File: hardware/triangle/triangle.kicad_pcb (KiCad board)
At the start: 4 copper layers, 100 x 86.6 mm, 60 parts, among them J1 Conn_01x02_Socket, J2 Conn_01x02_Socket

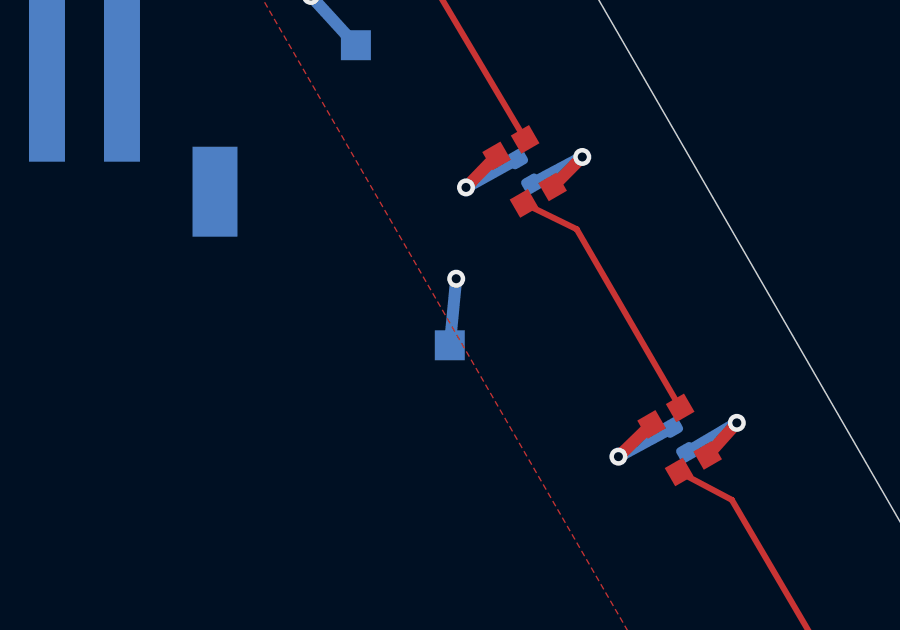
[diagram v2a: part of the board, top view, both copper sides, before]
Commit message: remove unnecessary test pad and add silkscreen for sockets
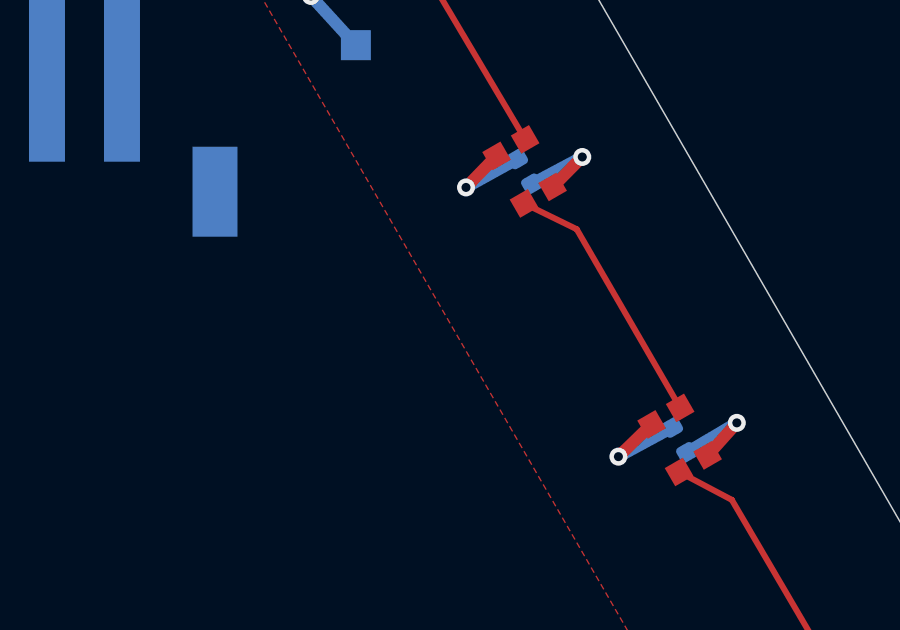
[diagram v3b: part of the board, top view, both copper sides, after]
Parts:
- removed TP2-GND1: TestPoint, TestPoint:TestPoint_Pad_1.0x1.0mm
- renumbered TP3-LED_DATA_IN1 to TP2-LED_DATA_IN1, TP4-LED_DATA_OUT1 to TP3-LED_DATA_OUT1
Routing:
- net GND: track 85.9 -> 83.7 mm, vias 26 -> 25
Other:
- board text added: "DATA"
- board text added: "POWER"
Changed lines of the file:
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@@
 		(descr "SMD rectangular pad as test Point, square 1.0mm side length")
 		(tags "test point SMD pad rectangle square")
-		(property "Reference" "TP3-LED_DATA_IN1"
-			(at 2.14597 2.509828 180)
+		(property "Reference" "TP2-LED_DATA_IN1"
+			(at 7.768737 2.304963 180)
 			(layer "B.SilkS")
 			(effects
@@
 		)
 	)
-	(footprint "TestPoint:TestPoint_Pad_1.0x1.0mm"
-		(layer "B.Cu")
-		(at 168.177353 114.994019)
-		(descr "SMD rectangular pad as test Point, square 1.0mm side length")
-		(tags "test point SMD pad rectangle square")
-		(property "Reference" "TP2-GND1"
-			(at 0 1.448 180)
-			(layer "B.SilkS")
-			(effects
-				(font
-					(size 1 1)
-					(thickness 0.15)
-				)
-				(justify mirror)
-			)
-		)
-		(property "Value" "TestPoint"
-			(at 0 -1.55 180)
-			(layer "B.Fab")
-			(effects
-				(font
-					(size 1 1)
-					(thickness 0.15)
-				)
-				(justify mirror)
-			)
-		)
-		(property "Datasheet" ""
-			(at 0 0 180)
-			(unlocked yes)
-			(layer "B.Fab")
-			(hide yes)
-			(effects
-				(font
-					(size 1.27 1.27)
-					(thickness 0.15)
-				)
-				(justify mirror)
-			)
-		)
-		(property "Description" "test point"
-			(at 0 0 180)
-			(unlocked yes)
-			(layer "B.Fab")
-			(hide yes)
-			(effects
-				(font
-					(size 1.27 1.27)
-					(thickness 0.15)
-				)
-				(justify mirror)
-			)
-		)
-		(property ki_fp_filters "Pin* Test*")
-		(sheetname "/")
-		(sheetfile "triangle.kicad_sch")
-		(units
-			(unit
-				(name "A")
-				(pins "1")
-			)
-		)
-		(duplicate_pad_numbers_are_jumpers no)
-		(fp_line
-			(start -0.7 -0.7)
-			(end -0.7 0.7)
-			(stroke
-				(width 0.12)
-				(type solid)
-			)
-			(layer "B.SilkS")
-		)
-		(fp_line
-			(start -0.7 0.7)
-			(end 0.7 0.7)
-			(stroke
-				(width 0.12)
-				(type solid)
-			)
-			(layer "B.SilkS")
-		)
-		(fp_line
-			(start 0.7 -0.7)
-			(end -0.7 -0.7)
-			(stroke
-				(width 0.12)
-				(type solid)
-			)
-			(layer "B.SilkS")
-		)
-		(fp_line
-			(start 0.7 0.7)
-			(end 0.7 -0.7)
-			(stroke
-				(width 0.12)
-				(type solid)
-			)
-			(layer "B.SilkS")
-		)
-		(fp_line
-			(start -1 1)
-			(end -1 -1)
-			(stroke
-				(width 0.05)
-				(type solid)
-			)
-			(layer "B.CrtYd")
-		)
-		(fp_line
-			(start -1 1)
-			(end 1 1)
-			(stroke
-				(width 0.05)
-				(type solid)
-			)
-			(layer "B.CrtYd")
-		)
-		(fp_line
-			(start 1 -1)
-			(end -1 -1)
-			(stroke
-				(width 0.05)
-				(type solid)
-			)
-			(layer "B.CrtYd")
-		)
-		(fp_line
-			(start 1 -1)
-			(end 1 1)
-			(stroke
-				(width 0.05)
-				(type solid)
-			)
-			(layer "B.CrtYd")
-		)
-		(fp_text user "${REFERENCE}"
-			(at 0 1.45 180)
-			(layer "B.Fab")
-			(effects
-				(font
-					(size 1 1)
-					(thickness 0.15)
-				)
-				(justify mirror)
-			)
-		)
-		(pad "1" smd rect
-			(at 0 0)
-			(size 1 1)
-			(layers "B.Cu" "B.Mask")
-			(net "GND")
-			(pinfunction "1_1")
-			(pintype "passive")
-		)
-		(embedded_fonts no)
-	)
 	(footprint "footprints:CONN-SMD_B2B-PH-SM4-TBT-LF-SN"
 		(layer "B.Cu")
@@
 				(font
 					(size 1.27 1.27)
+					(thickness 0.15)
 				)
 			)
@@
 				(font
 					(size 1.27 1.27)
+					(thickness 0.15)
 				)
 			)
@@
 		(descr "SMD rectangular pad as test Point, square 1.0mm side length")
 		(tags "test point SMD pad rectangle square")
-		(property "Reference" "TP4-LED_DATA_OUT1"
+		(property "Reference" "TP3-LED_DATA_OUT1"
 			(at 9.150116 0.172102 180)
 			(layer "B.SilkS")
@@
 		(layer "Edge.Cuts")
 	)
+	(gr_text "DATA"
+		(at 138.826309 123.211051 0)
+		(layer "B.SilkS")
+		(effects
+			(font
+				(size 1.5 1.5)
+				(thickness 0.3)
+				(bold yes)
+			)
+			(justify left bottom mirror)
+		)
+	)
+	(gr_text "POWER"
+		(at 159.990256 114.835091 0)
+		(layer "B.SilkS")
+		(effects
+			(font
+				(size 1.5 1.5)
+				(thickness 0.3)
+				(bold yes)
+			)
+			(justify left bottom mirror)
+		)
+	)
 	(segment
 		(start 116.350567 141.095301)
@@
 	)
 	(via
-		(at 168.390091 112.775809)
-		(size 0.6)
-		(drill 0.3)
-		(layers "F.Cu" "B.Cu")
-		(net "GND")
-	)
-	(via
 		(at 182.587218 143.028772)
 		(size 0.6)
@@
 		(width 0.4)
 		(layer "B.Cu")
-		(net "GND")
-	)
-	(segment
-		(start 168.177353 114.994019)
-		(end 168.390091 112.775809)
-		(width 0.4)
-		(layer "B.Cu")

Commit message: holes only.
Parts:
- H1, H2, H3: footprint footprints:SMD_BD5.6-L5.6-W5.6-D4.1 -> MountingHole:MountingHole_3.2mm_M3

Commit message: updating components on triangle board - in progress
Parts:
- added R5: 5.1kΩ, Resistor_SMD:R_0603_1608Metric, B.Cu at (156.7, 124.7)
- added R6: 5.1kΩ, Resistor_SMD:R_0603_1608Metric, B.Cu at (156.7, 122.2)
- added R7: 5.1kΩ, Resistor_SMD:R_0603_1608Metric, B.Cu at (156.7, 119.7)
- added R8: 5.1kΩ, Resistor_SMD:R_0603_1608Metric, B.Cu at (156.7, 117.2)
- J1: value Conn_01x02_Socket -> USB_C_Receptacle_USB2.0_16P; footprint footprints:CONN-SMD_B2B-PH-SM4-TBT-LF-SN -> footprints:TYPE-C-SMD_USB4120-03-C
- J2: value Conn_01x02_Socket -> USB_C_Receptacle_USB2.0_16P; footprint footprints:CONN-SMD_ZX-XH2.54-2PLT -> footprints:TYPE-C-SMD_USB4120-03-C
- moved C25 34.1 mm to (156.2, 135.5), turned to 90 degrees
- moved TP2-LED_DATA_IN1 30.4 mm to (144.2, 107.3)
- moved J2 24.3 mm to (135.4, 121.0), turned to 0 degrees
- moved TP3-LED_DATA_OUT1 23.1 mm to (141.7, 112.0)
- moved J1 15.7 mm to (149.8, 135.6), turned to -90 degrees
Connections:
- C25 pad 1: 5V Power -> GND
- C25 pad 2: Net-(J2-Pin_1) -> 12V Power
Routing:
- net LED_DATA_OUT: track 43.8 -> 24.8 mm
- net LED_DATA_IN: track 37.8 -> 20.7 mm
- net Net-(J2-Pin_1): track 4.56 -> 0.00 mm
- net GND: track 83.7 -> 81.8 mm, vias 25 -> 28
- net 5V Power: track 100.2 -> 98.2 mm, vias 26 -> 25
- added copper zone on In2.Cu, net 12V Power
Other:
- board text removed: "DATA"
- board text removed: "POWER"

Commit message: trying and failing to fix the usb-c
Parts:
- TP1-5V1, TP2-LED_DATA_IN1: footprint TestPoint:TestPoint_Pad_1.0x1.0mm -> TestPoint:TestPoint_Pad_D2.0mm
- TP3_LED_DATA_OUT: renamed from TP3-LED_DATA_OUT1; footprint TestPoint:TestPoint_Pad_1.0x1.0mm -> TestPoint:TestPoint_Pad_D2.0mm
- moved TP2-LED_DATA_IN1 37.4 mm to (144.5, 144.7)
- moved R5 26.7 mm to (131.8, 134.5)
- moved R7 23.6 mm to (133.7, 125.1)
- moved R8 19.7 mm to (137.0, 117.1), turned to 180 degrees
- moved R6 17.9 mm to (141.4, 131.4), turned to -90 degrees
- moved C25 14.6 mm to (141.8, 137.6)
- moved J1 12.5 mm to (137.3, 135.2)
- moved TP3_LED_DATA_OUT 11.5 mm to (130.3, 113.3)
- moved J2 0.05 mm to (135.4, 121.0)
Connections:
- J1 pad 0: (no net) -> GND
- J2 pad 0: (no net) -> GND
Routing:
- net LED_DATA_IN: track 20.7 -> 47.5 mm
- net LED_DATA_OUT: track 24.8 -> 46.8 mm
- net 12V Power: track 0.00 -> 16.5 mm, vias 0 -> 4
- net GND: track 81.8 -> 95.9 mm, vias 28 -> 24
- net Net-(J1-CC2): track 0.00 -> 5.33 mm
- net Net-(J1-CC1): track 0.00 -> 3.81 mm
- net Net-(J2-CC1): track 0.00 -> 3.31 mm
- net Net-(J2-CC2): track 0.00 -> 3.13 mm

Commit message: Update triangle.kicad_pcb
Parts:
- moved J2 7.20 mm to (142.4, 119.6)
- moved R7 7.20 mm to (140.8, 123.7)
- moved R8 7.20 mm to (144.0, 115.7)
- moved C25 5.35 mm to (146.7, 135.4)
- moved J1 5.35 mm to (142.2, 133.0)
- moved R5 5.35 mm to (136.7, 132.3)
- moved R6 5.35 mm to (146.2, 129.2)
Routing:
- net LED_DATA_OUT: track 46.8 -> 54.3 mm
- net LED_DATA_IN: track 47.5 -> 52.9 mm
- removed copper zone on F.Cu, net (none)

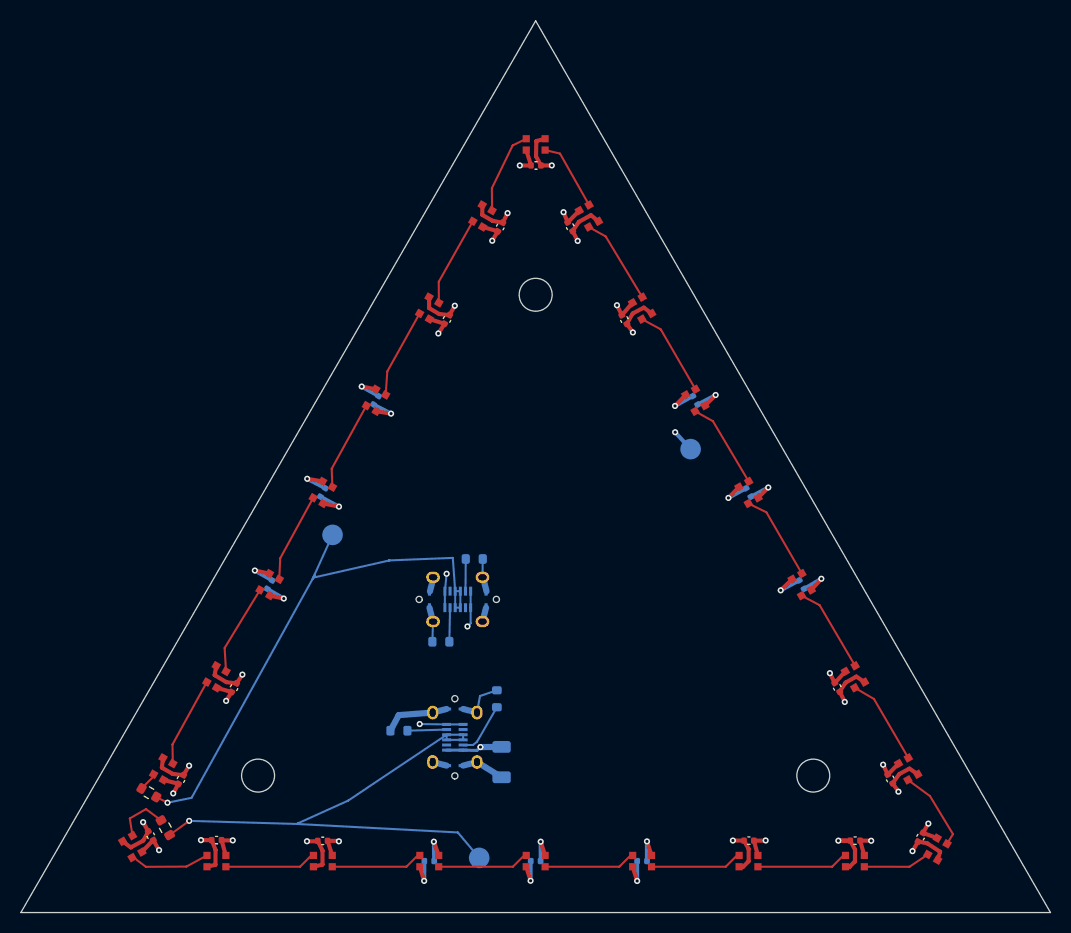
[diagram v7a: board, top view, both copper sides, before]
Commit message: redraw fill zone
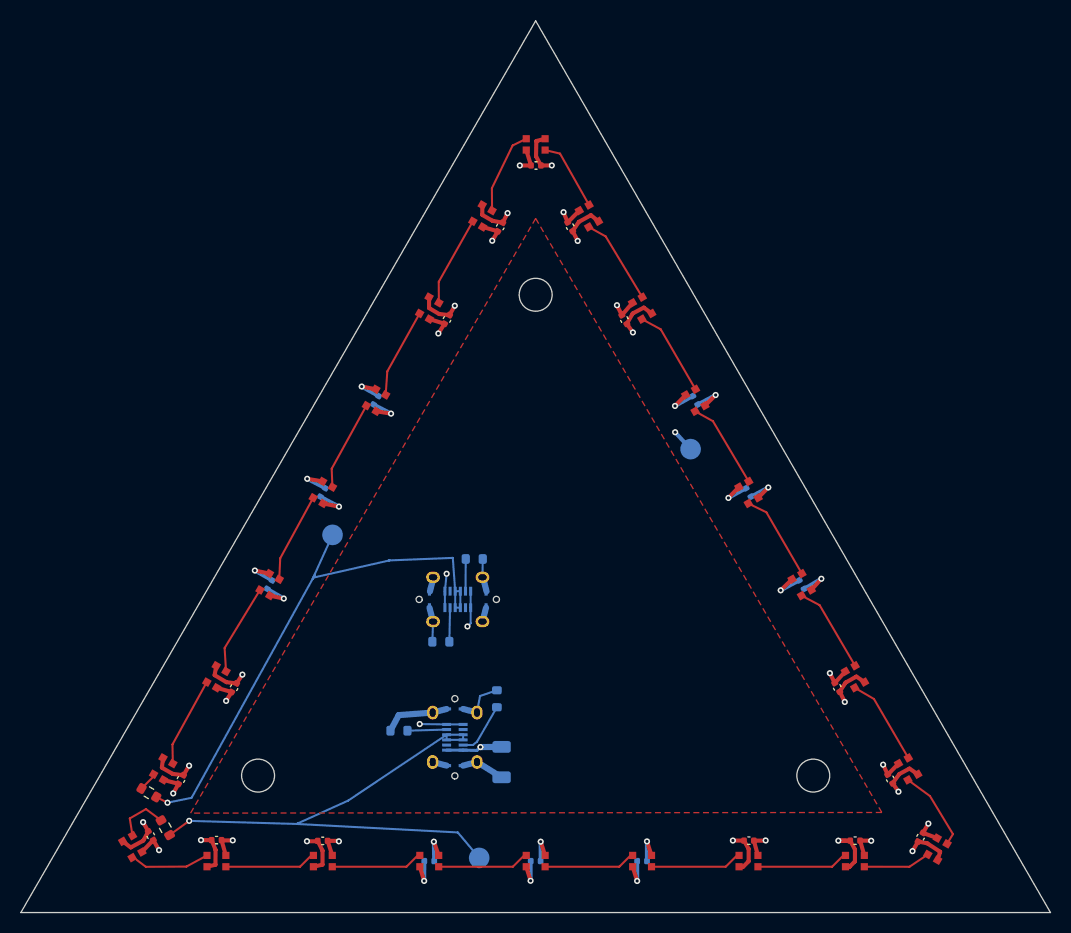
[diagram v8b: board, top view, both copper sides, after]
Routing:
- added copper zone on F.Cu, net (none)
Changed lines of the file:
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@@
-	)
-	(gr_line
-		(start 149.952411 82.746544)
-		(end 116.64826 140.34659)
-		(stroke
-			(width 0.05)
-			(type default)
-		)
-		(layer "Eco1.User")
-	)
-	(gr_line
-		(start 183.252982 140.312305)
-		(end 149.952411 82.746544)
-		(stroke
-			(width 0.05)
-			(type default)
-		)
-		(layer "Eco1.User")
 	)
 	(gr_line
@@
 	)
 	(zone
+		(layer "F.Cu")
+		(hatch none 0.5)
+		(connect_pads
+			(clearance 0)
+		)
+		(min_thickness 0.25)
+		(keepout
+			(tracks allowed)
+			(vias allowed)
+			(pads allowed)
+			(copperpour not_allowed)
+			(footprints allowed)
+		)
+		(placement
+			(enabled no)
+			(sheetname "/")
+		)
+		(fill
+			(thermal_gap 0.5)
+			(thermal_bridge_width 0.5)
+			(island_removal_mode 1)
+		)
+		(polygon
+			(pts
+				(arc
+					(start 143.978757 133.941268)
+					(mid 145.313329 133.941268)
+					(end 143.978757 133.941268)
+				)
+			)
+		)
+	)
+	(zone
+		(layer "F.Cu")
+		(hatch none 0.5)
+		(priority 1)
+		(connect_pads
+			(clearance 0.5)
+		)
+		(min_thickness 0.25)
+		(fill yes
+			(thermal_gap 0.5)
+			(thermal_bridge_width 0.5)
+			(island_removal_mode 1)
+		)
+		(polygon
+			(pts
+				(xy 183.613508 140.280376) (xy 116.483275 140.341654) (xy 150 82.586981) (xy 183.615399 140.275647)
+			)
+		)
+	)
+	(zone
